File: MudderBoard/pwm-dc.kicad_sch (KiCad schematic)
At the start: 19 parts, among them K1 AZ2850-2A-12DE, Q5 NPN, U6 UA741, U7 LM339, U8 UA741

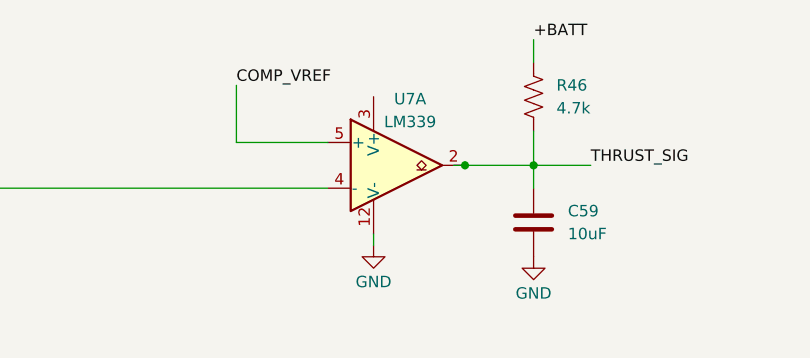
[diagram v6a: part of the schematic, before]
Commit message: AddedPWM-DC footprints
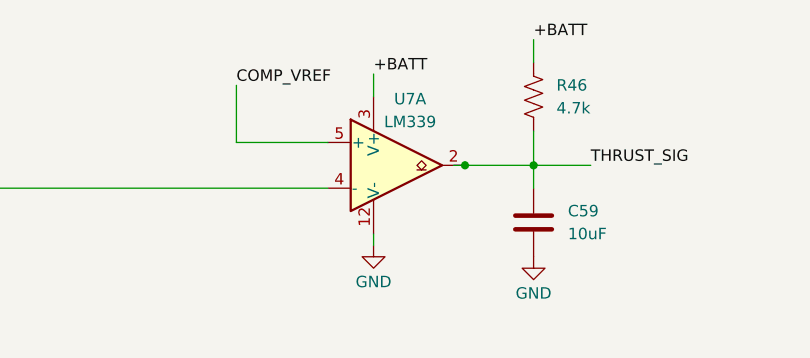
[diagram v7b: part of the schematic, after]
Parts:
- C18, C58: footprint (none) -> PDC_Foot:CAPC2012X140N
- C59, C61: footprint (none) -> PDC_Foot:CAPC2012X135N
- D7: footprint (none) -> PDC_Foot:SOT_45-M3&slash_I_VIS
- K1: footprint AZ28502A12DE -> AZ2850-2A-12DE:AZ28502A12DE
- Q5: footprint (none) -> PDC_Foot:SOT95P237X111-3N
- R42, R43: footprint (none) -> PDC_Foot:RESC1608X55N
- R44, R45: footprint (none) -> PDC_Foot:RES_ERA6AEB1581V
- R46, R48: footprint (none) -> PDC_Foot:RESC2012X65N
- R51: footprint (none) -> Lidar_Foot:RESC1607X60N
- U6, U8: footprint (none) -> PDC_Foot:SOIC127P599X175-8N
- U7: footprint (none) -> Package_SO:TSSOP-14_4.4x5mm_P0.65mm
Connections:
- net +BATT: now also U7.3 (V+)
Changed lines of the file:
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@@
 	(wire
 		(pts
+			(xy 147.32 20.32) (xy 147.32 22.86)
+		)
+		(stroke
+			(width 0)
+			(type default)
+		)
+	)
+	(wire
+		(pts
 			(xy 45.72 74.93) (xy 58.42 74.93)
 		)
@@
 		)
 	)
+	(label "+BATT"
+		(at 147.32 20.32 0)
+		(fields_autoplaced yes)
+		(effects
+			(font
+				(size 1.27 1.27)
+			)
+			(justify left bottom)
+		)
+	)
 	(symbol
 		(lib_id "power:GND")
@@
 			)
 		)
-		(property "Footprint" ""
+		(property "Footprint" "PDC_Foot:SOIC127P599X175-8N"
 			(at 91.44 76.2 0)
 			(effects
@@
 			)
 		)
-		(property "Datasheet" ""
+		(property "Datasheet" "UA741CDR"
 			(at 93.98 73.66 0)
 			(effects
@@
 			)
 		)
-		(property "Footprint" ""
+		(property "Footprint" "PDC_Foot:RES_ERA6AEB1581V"
 			(at 63.754 166.116 90)
 			(effects
@@
 			)
 		)
-		(property "Datasheet" "~"
+		(property "Datasheet" "ERA-6AEB1581V"
 			(at 64.77 166.37 0)
 			(effects
@@
 			)
 		)
-		(property "Footprint" ""
+		(property "Footprint" "PDC_Foot:SOT_45-M3&slash_I_VIS"
 			(at 121.92 120.65 0)
 			(effects
@@
 			)
 		)
-		(property "Datasheet" "~"
+		(property "Datasheet" "V40DL45-M3/I"
 			(at 121.92 120.65 0)
 			(effects
@@
 			)
 		)
-		(property "Footprint" ""
+		(property "Footprint" "Package_SO:TSSOP-14_4.4x5mm_P0.65mm"
 			(at 148.59 27.94 0)
 			(effects
@@
 			)
 		)
-		(property "Footprint" ""
+		(property "Footprint" "PDC_Foot:RES_ERA6AEB1581V"
 			(at 63.754 177.546 90)
 			(effects
@@
 			)
 		)
-		(property "Datasheet" "~"
+		(property "Datasheet" "ERA-6AEB1581V"
 			(at 64.77 177.8 0)
 			(effects
@@
 			)
 		)
-		(property "Footprint" ""
+		(property "Footprint" "Lidar_Foot:RESC1607X60N"
 			(at 71.374 137.414 90)
 			(effects
@@
 			)
 		)
-		(property "Datasheet" "~"
+		(property "Datasheet" "RC0603FR-072K4L"
 			(at 71.12 138.43 0)
 			(effects
@@
 			)
 		)
-		(property "Footprint" ""
+		(property "Footprint" "Package_SO:TSSOP-14_4.4x5mm_P0.65mm"
 			(at 30.48 177.8 0)
 			(effects
@@
 			)
 		)
-		(property "Footprint" ""
+		(property "Footprint" "PDC_Foot:RESC2012X65N"
 			(at 194.564 67.056 90)
 			(effects
@@
 			)
 		)
-		(property "Datasheet" "~"
+		(property "Datasheet" "RMCF0805JT4K70"
 			(at 195.58 67.31 0)
 			(effects
@@
 			)
 		)
-		(property "Footprint" "AZ28502A12DE"
+		(property "Footprint" "AZ2850-2A-12DE:AZ28502A12DE"
 			(at 158.75 207.95 0)
 			(effects
@@
 			)
 		)
-		(property "Footprint" ""
+		(property "Footprint" "PDC_Foot:SOT95P237X111-3N"
 			(at 152.4 138.43 0)
 			(effects
@@
 			)
 		)
-		(property "Datasheet" "https://ngspice.sourceforge.io/docs/ngspice-html-manual/manual.xhtml#cha_BJTs"
+		(property "Datasheet" "BCW65ALT1G"
 			(at 152.4 138.43 0)
 			(effects
@@
 			)
 		)
-		(property "Footprint" ""
+		(property "Footprint" "Package_SO:TSSOP-14_4.4x5mm_P0.65mm"
 			(at 148.59 72.39 0)
 			(effects
@@
 			)
 		)
-		(property "Footprint" ""
+		(property "Footprint" "PDC_Foot:RESC1608X55N"
 			(at 43.434 29.464 90)
 			(effects
@@
 			)
 		)
-		(property "Datasheet" "~"
+		(property "Datasheet" "RT0603BRC07500RL"
 			(at 43.18 30.48 0)
 			(effects
@@
 			)
 		)
-		(property "Footprint" ""
+		(property "Footprint" "PDC_Foot:CAPC2012X135N"
 			(at 196.5452 85.09 0)
 			(effects
@@
 			)
 		)
-		(property "Datasheet" "~"
+		(property "Datasheet" "CL21A106KOQNNNE"
 			(at 195.58 81.28 0)
 			(effects
@@
 			)
 		)
-		(property "Footprint" ""
+		(property "Footprint" "PDC_Foot:CAPC2012X140N"
 			(at 60.6552 41.91 0)
 			(effects
@@
 			)
 		)
-		(property "Datasheet" "~"
+		(property "Datasheet" "CL21A475KAQNNNE"
 			(at 59.69 38.1 0)
 			(effects
@@
 			)
 		)
-		(property "Footprint" ""
+		(property "Footprint" "PDC_Foot:RESC1608X55N"
 			(at 42.164 73.914 90)
 			(effects
@@
 			)
 		)
-		(property "Datasheet" "~"
+		(property "Datasheet" "RT0603BRC07500RL"
 			(at 41.91 74.93 0)
 			(effects
@@
 			)
 		)
-		(property "Footprint" ""
+		(property "Footprint" "PDC_Foot:RESC2012X65N"
 			(at 164.084 22.606 90)
 			(effects
@@
 			)
 		)
-		(property "Datasheet" "~"
+		(property "Datasheet" "RMCF0805JT4K70"
 			(at 165.1 22.86 0)
 			(effects
@@
 			)
 		)
-		(property "Footprint" ""
+		(property "Footprint" "Package_SO:TSSOP-14_4.4x5mm_P0.65mm"
 			(at 148.59 27.94 0)
 			(effects
@@
 			)
 		)
-		(property "Footprint" ""
+		(property "Footprint" "Package_SO:TSSOP-14_4.4x5mm_P0.65mm"
 			(at 30.48 160.02 0)
 			(effects
@@
 			)
 		)
-		(property "Footprint" ""
+		(property "Footprint" "PDC_Foot:CAPC2012X140N"
 			(at 59.3852 86.36 0)
 			(effects
@@
 			)
 		)
-		(property "Datasheet" "~"
+		(property "Datasheet" "CL21A475KAQNNNE"
 			(at 58.42 82.55 0)
 			(effects
@@
 			)
 		)
-		(property "Footprint" ""
+		(property "Footprint" "PDC_Foot:SOIC127P599X175-8N"
 			(at 92.71 31.75 0)
 			(effects
@@
 			)
 		)
-		(property "Datasheet" ""
+		(property "Datasheet" "UA741CDR"
 			(at 95.25 29.21 0)
 			(effects
@@
 			)
 		)
-		(property "Footprint" ""
+		(property "Footprint" "PDC_Foot:CAPC2012X135N"
 			(at 166.0652 40.64 0)
 			(effects
@@
 			)
 		)
-		(property "Datasheet" "~"
+		(property "Datasheet" "CL21A106KOQNNNE"
 			(at 165.1 36.83 0)
 			(effects

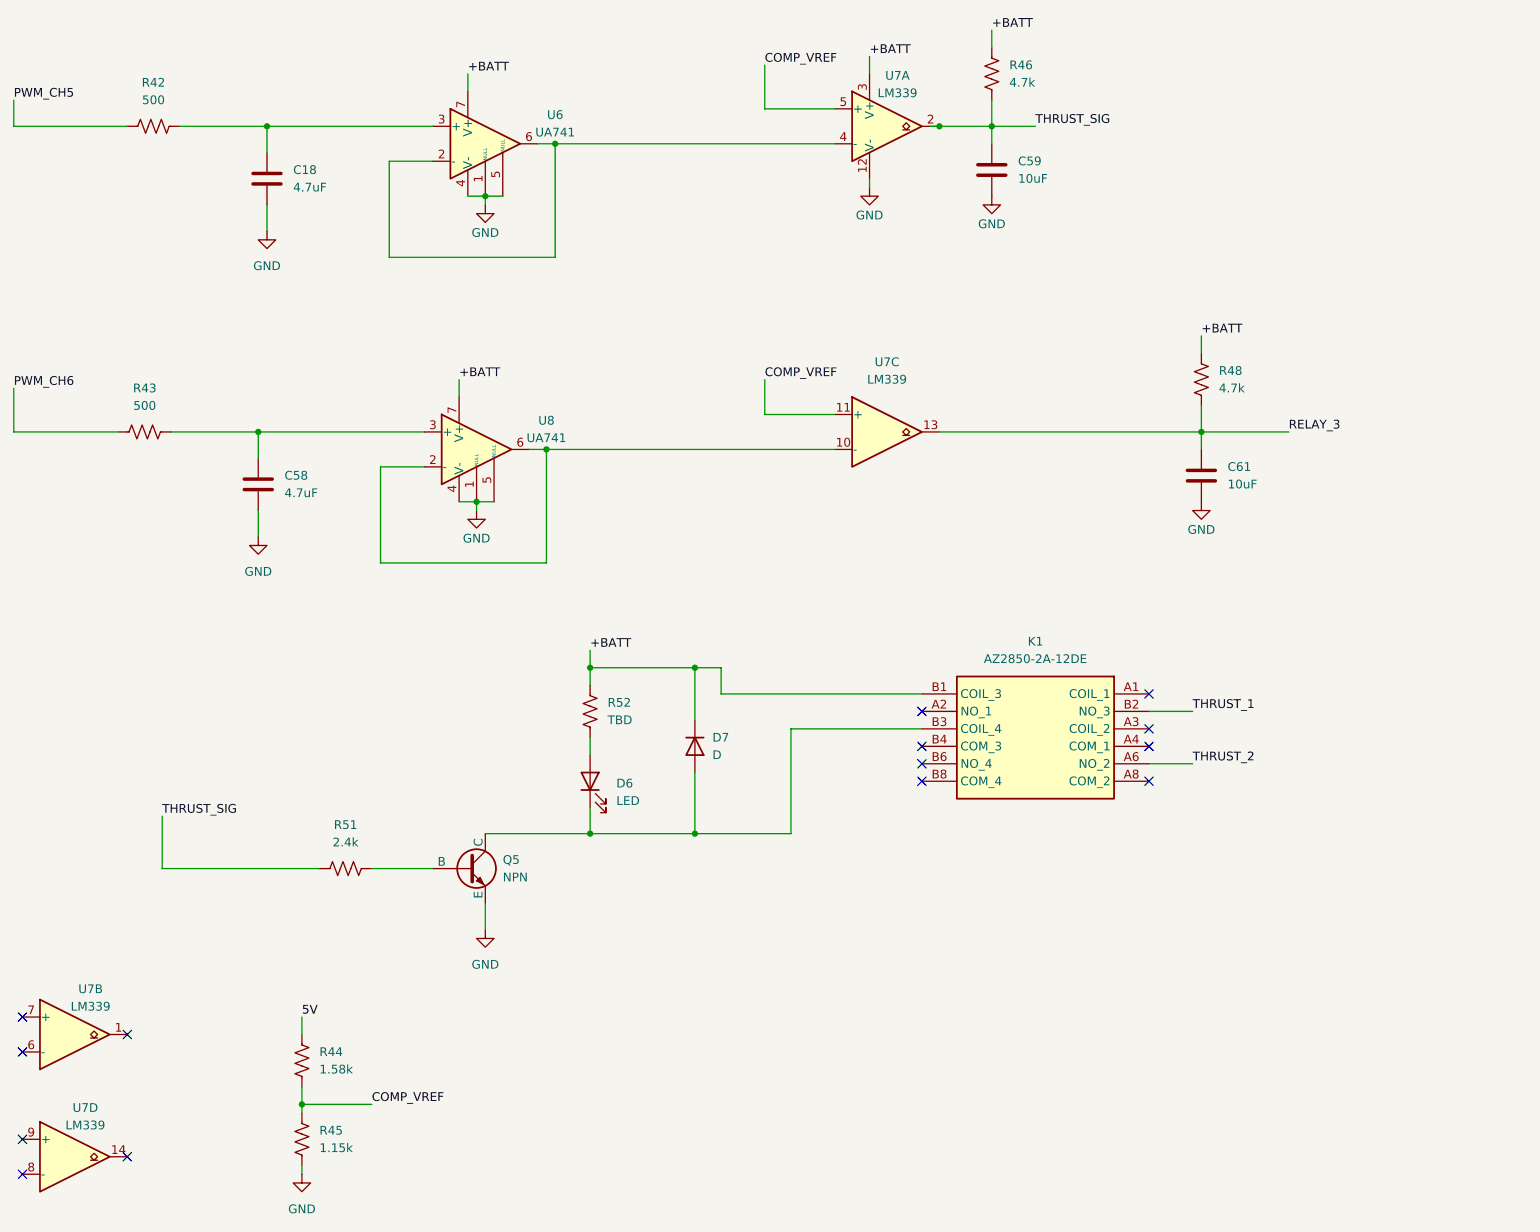
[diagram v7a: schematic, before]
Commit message: Imported footprints to layout
Colin - Make note of these

C30,C32 are generic 0805 caps
L4,L5 are basic insuctors, will need to change when we figure this situation out!

U8,U9 changed to same boost IC as Lidar - these are the same right?
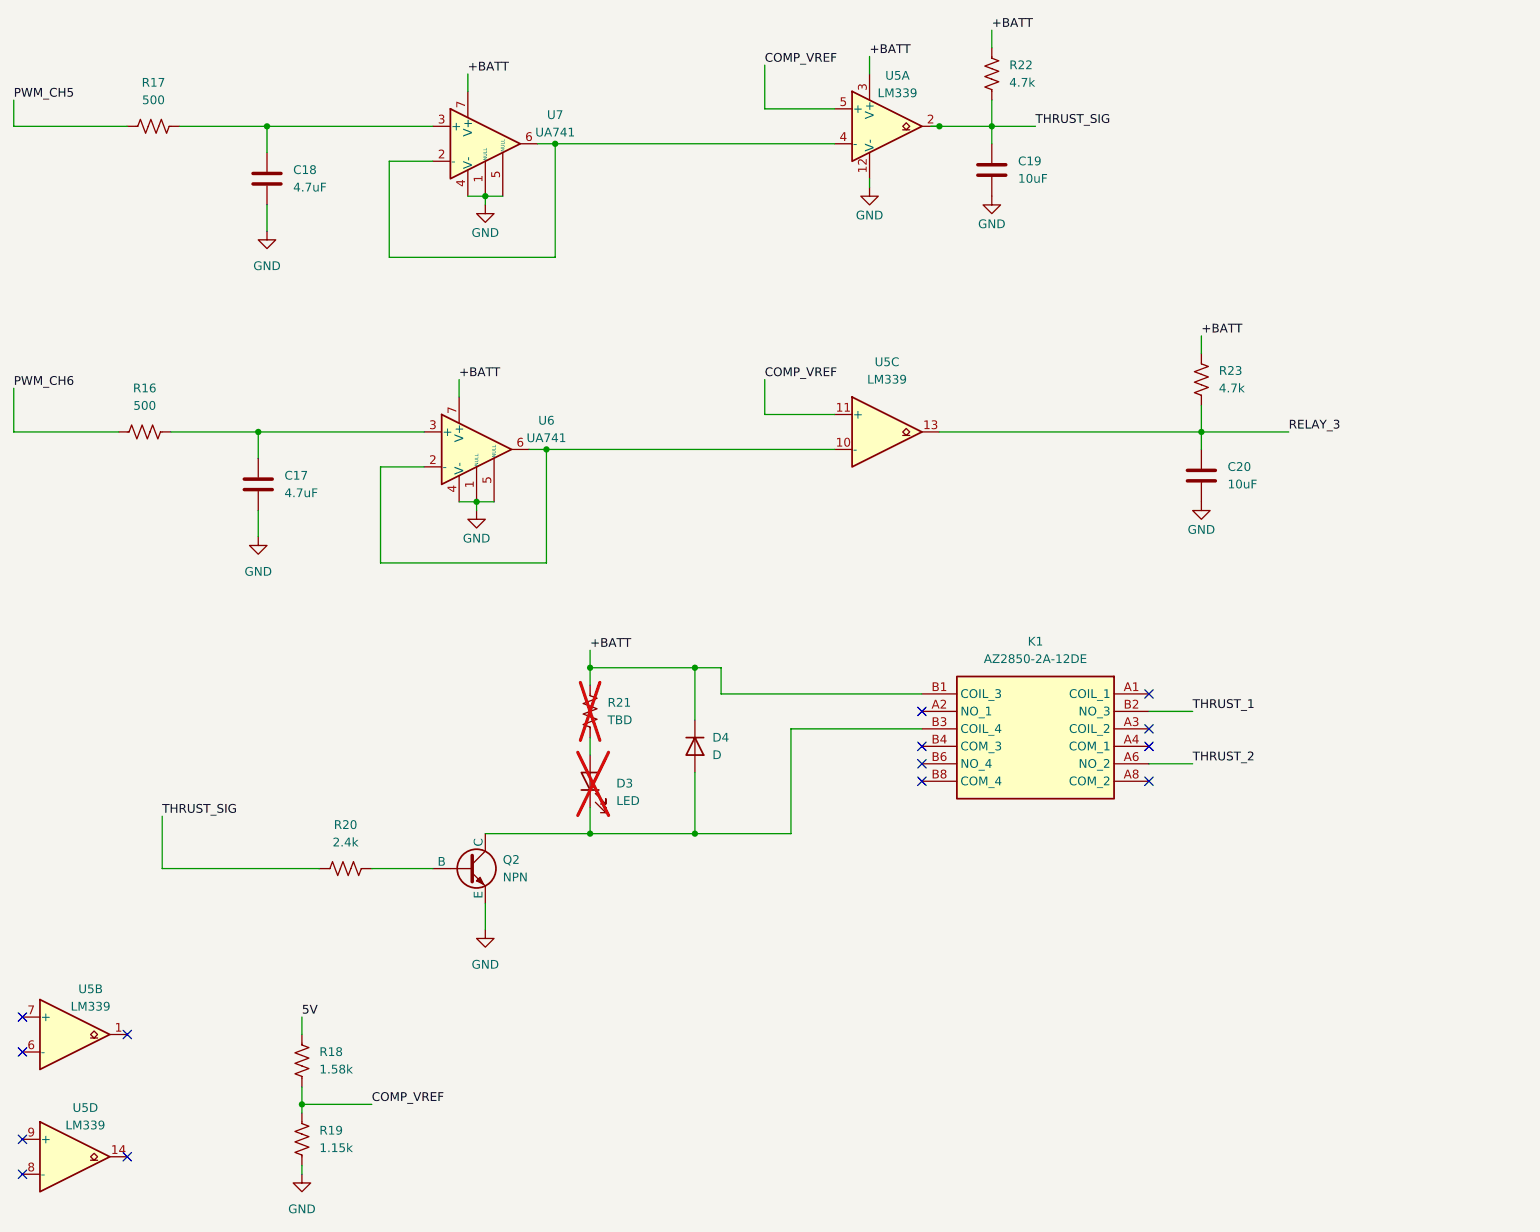
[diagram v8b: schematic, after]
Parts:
- D3: renamed from D6; now not fitted
- R21: renamed from R52; now not fitted
- renumbered C58 to C17, C59 to C19, C61 to C20, D7 to D4, Q5 to Q2, R43 to R16, R42 to R17, R44 to R18, R45 to R19, R51 to R20, R46 to R22, R48 to R23, U7 to U5, U8 to U6, U6 to U7
